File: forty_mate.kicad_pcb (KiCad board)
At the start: 2 copper layers, 247.5 x 76 mm, 95 parts, among them SW1 SW_Push, SW10 SW_Push, SW11 SW_Push, SW12 SW_Push, SW13 SW_Push, SW14 SW_Push, SW15 SW_Push, SW16 SW_Push, SW17 SW_Push, SW18 SW_Push, SW19 SW_Push, SW2 SW_Push, SW20 SW_Push, SW21 SW_Push, SW22 SW_Push, SW23 SW_Push, SW24 SW_Push, SW25 SW_Push, SW26 SW_Push, SW27 SW_Push, SW28 SW_Push, SW29 SW_Push, SW3 SW_Push, SW30 SW_Push, SW31 SW_Push, SW32 SW_Push, SW33 SW_Push, SW34 SW_Push, SW35 SW_Push, SW36 SW_Push, SW37 SW_Push, SW38 SW_Push, SW39 SW_Push, SW4 SW_Push, SW40 SW_Push, SW41 SW_Push, SW42 SW_Push, SW43 SW_Push, SW44 SW_SPDT, SW5 SW_Push, SW6 SW_Push, SW7 SW_Push, SW8 SW_Push, SW9 SW_Push, U1 Micon_BLEMicroPro

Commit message: gasket case version
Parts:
- added REF**: masro_poron, forty_mate:masro_poron, F.Cu at (260.6, 57.0)
- added REF**: masro_poron, forty_mate:masro_poron, F.Cu at (95.5, 57.0)
- added REF**: masro_poron, forty_mate:masro_poron, F.Cu at (80.5, 57.0)
- added REF**: masro_poron, forty_mate:masro_poron, F.Cu at (178.0, 138.2)
- added REF**: masro_poron, forty_mate:masro_poron, F.Cu at (178.0, 57.0)
- added REF**: masro_poron, forty_mate:masro_poron, F.Cu at (122.0, 138.2)
- added REF**: masro_poron, forty_mate:masro_poron, F.Cu at (204.6, 57.0)
- added REF**: masro_poron, forty_mate:masro_poron, F.Cu at (39.5, 57.0)
- added REF**: masro_poron, forty_mate:masro_poron, F.Cu at (54.5, 57.0)
- added REF**: masro_poron, forty_mate:masro_poron, F.Cu at (95.5, 138.2)
- added REF**: masro_poron, forty_mate:masro_poron, F.Cu at (163.0, 138.2)
- added REF**: masro_poron, forty_mate:masro_poron, F.Cu at (219.6, 57.0)
- added REF**: masro_poron, forty_mate:masro_poron, B.Cu at (69.5, 138.2)
- added REF**: masro_poron, forty_mate:masro_poron, F.Cu at (163.0, 57.0)
- added REF**: masro_poron, forty_mate:masro_poron, F.Cu at (137.0, 57.0)
- added REF**: masro_poron, forty_mate:masro_poron, F.Cu at (204.6, 138.2)
- added REF**: masro_poron, forty_mate:masro_poron, F.Cu at (137.0, 138.2)
- added REF**: masro_poron, forty_mate:masro_poron, F.Cu at (230.6, 138.2)
- added REF**: masro_poron, forty_mate:masro_poron, F.Cu at (245.6, 57.0)
- added REF**: masro_poron, forty_mate:masro_poron, F.Cu at (122.0, 57.0)
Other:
- board text added: "User1: general case plate line User2: split line User3: switch plate line User4: poron"
- board text removed: "User1: outline User2: outline 2 (split)"

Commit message: kari kansei
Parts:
- removed BT2: Battery_Cell, kbd_Parts:Battery_ali_CR1632
- removed C2: C_Polarized_Small, kbd_Parts:Capacitor_1206
- removed D45: D_Schottky, forty_mate:Diode_SMD
- removed G***: LOGO, forty_mate:Silk_Title
- removed the REF** at (260.6, 57.0)
- removed the REF** at (95.5, 57.0)
- removed the REF** at (80.5, 57.0)
- removed the REF** at (178.0, 138.2)
- removed the REF** at (178.0, 57.0)
- removed the REF** at (122.0, 138.2)
- removed the REF** at (204.6, 57.0)
- removed the REF** at (39.5, 57.0)
- removed the REF** at (54.5, 57.0)
- removed the REF** at (95.5, 138.2)
- removed the REF** at (163.0, 138.2)
- removed the REF** at (219.6, 57.0)
- removed the REF** at (69.5, 138.2)
- removed the REF** at (163.0, 57.0)
- removed the REF** at (137.0, 57.0)
- removed the REF** at (204.6, 138.2)
- removed the REF** at (137.0, 138.2)
- removed the REF** at (230.6, 138.2)
- removed the REF** at (245.6, 57.0)
- removed the REF** at (122.0, 57.0)
- added REF**: MountingHole_2.1mm, MountingHole:MountingHole_2.1mm, F.Cu at (59.5, 133.3)
- added REF**: MountingHole_2.1mm, MountingHole:MountingHole_2.1mm, F.Cu at (107.2, 116.7)
- added REF**: MountingHole_2.1mm, MountingHole:MountingHole_2.1mm, F.Cu at (50.0, 97.6)
- added REF**: MountingHole_2.1mm, MountingHole:MountingHole_2.1mm, F.Cu at (235.7, 119.1)
- added REF**: MountingHole_2.1mm, MountingHole:MountingHole_2.1mm, F.Cu at (59.5, 119.1)
- added REF**: MountingHole_2.1mm, MountingHole:MountingHole_2.1mm, F.Cu at (242.9, 97.6)
- added REF**: MountingHole_2.1mm, MountingHole:MountingHole_2.1mm, F.Cu at (235.7, 133.3)
- added REF**: MountingHole_2.1mm, MountingHole:MountingHole_2.1mm, F.Cu at (188.1, 116.7)
- added SW45: SW_Push, kbd_Parts:ResetSW, F.Cu at (235.7, 126.2)
- C1, SW44: moved to B.Cu
- D44: footprint forty_mate:Diode_SMD -> forty_mate:Diode_SMD_S-FLAT
- SW12, SW35, SW38: footprint kbd_SW:CherryMX_Hotswap_1u -> kbd_SW:CherryMX_Hotswap_1.25u
- SW14, SW39: footprint kbd_SW:CherryMX_Hotswap_1.25u -> kbd_SW:CherryMX_Hotswap_1u
- SW23, SW43: footprint kbd_SW:CherryMX_Hotswap_1u -> kbd_SW:CherryMX_Hotswap_1.75u
- SW25, SW26: footprint kbd_SW:CherryMX_Hotswap_1.75u -> kbd_SW:CherryMX_Hotswap_1u
- SW36: footprint kbd_SW:CherryMX_Hotswap_1u -> kbd_SW:CherryMX_Hotswap_2u_Rev
- SW37: footprint kbd_SW:CherryMX_Hotswap_1.25u -> kbd_SW:CherryMX_Hotswap_2.25u_Rev
- SW40: footprint kbd_SW:CherryMX_Hotswap_2u_Rev -> kbd_SW:CherryMX_Hotswap_1u
- SW41: footprint kbd_SW:CherryMX_Hotswap_2.25u_Rev -> kbd_SW:CherryMX_Hotswap_1u
- moved SW44 243.6 mm to (271.5, 126.2)
- moved BT1 216.7 mm to (45.2, 126.2), turned to 0 degrees
- moved U1 209.5 mm to (254.8, 126.2), turned to -90 degrees
- moved SW12 208.0 mm to (38.1, 88.1)
- moved D12 208.0 mm to (45.2, 92.9)
- moved SW13 205.7 mm to (59.5, 88.1)
- moved D13 205.7 mm to (66.7, 92.9)
- moved C1 196.4 mm to (258.6, 128.6), turned to 180 degrees
- moved SW23 170.1 mm to (42.9, 107.2)
- moved SW25 170.1 mm to (88.1, 107.2)
- moved D25 170.1 mm to (95.2, 111.9)
- moved D23 170.1 mm to (50.0, 111.9)
- moved SW24 163.0 mm to (69.1, 107.2)
- moved D24 163.0 mm to (76.2, 111.9)
- moved SW34 130.0 mm to (73.8, 126.2)
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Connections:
- D12 pad 1: row0 -> row1
- D13 pad 1: row0 -> row1
- D23 pad 1: row1 -> row2
- D24 pad 1: row1 -> row2
- D25 pad 1: row1 -> row2
- D34 pad 1: row2 -> row3
- D35 pad 1: row2 -> row3
- D36 pad 1: row2 -> row3
- D37 pad 1: row2 -> row3
- SW12 pad 1: col11 -> col0
- SW13 pad 1: col12 -> col1
- SW14 pad 1: col0 -> col2
- SW15 pad 1: col1 -> col3
- SW16 pad 1: col2 -> col4
- SW17 pad 1: col3 -> col5
- SW18 pad 1: col4 -> col6
- SW19 pad 1: col5 -> col7
- SW20 pad 1: col6 -> col8
- SW21 pad 1: col7 -> col9
- SW22 pad 1: col8 -> col10
- SW23 pad 1: col9 -> col0
- SW24 pad 1: col10 -> col1
- SW25 pad 1: col12 -> col2
- SW26 pad 1: col0 -> col3
- SW27 pad 1: col2 -> col4
- SW28 pad 1: col3 -> col5
- SW29 pad 1: col4 -> col6
- SW30 pad 1: col5 -> col7
- SW31 pad 1: col6 -> col8
- SW32 pad 1: col7 -> col9
- SW33 pad 1: col8 -> col10
- SW34 pad 1: col9 -> col1
- SW35 pad 1: col10 -> col2
- SW36 pad 1: col11 -> col3
- SW37 pad 1: col12 -> col4
- SW38 pad 1: col2 -> col5
- SW39 pad 1: col3 -> col6
- SW40 pad 1: col5 -> col7
- SW41 pad 1: col7 -> col8
- U1 pad 10: col10 -> col9
- U1 pad 11: col11 -> col8
- U1 pad 12: col12 -> col7
- U1 pad 13: col3 -> unconnected-(U1-Pad13)
- U1 pad 14: col2 -> col0
- U1 pad 16: col0 -> col2
- U1 pad 2: col4 -> unconnected-(U1-Pad2)
- U1 pad 22: unconnected-(U1-Pad22) -> reset
- U1 pad 5: col5 -> col6
- U1 pad 6: col6 -> col5
- U1 pad 7: col7 -> col4
- U1 pad 8: col8 -> col3
- U1 pad 9: col9 -> col10
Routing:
- net col12: track 272.5 -> 0.00 mm, vias 7 -> 0
- net GND: track 0.00 -> 260.3 mm, vias 7 -> 0
- net col11: track 249.4 -> 0.00 mm, vias 6 -> 0
- net col3: track 104.2 -> 329.4 mm, vias 4 -> 6
- net col1: track 58.6 -> 282.0 mm, vias 2 -> 5
- net Net-(D44-Pad1): track 230.3 -> 10.5 mm, vias 3 -> 0
- net Net-(BT1-Pad1): track 26.3 -> 231.9 mm
- net col0: track 74.5 -> 278.2 mm, vias 3 -> 4
- net col2: track 101.4 -> 265.3 mm, vias 4 -> 5
- net col4: track 177.8 -> 324.8 mm, vias 5 -> 6
- net col9: track 269.8 -> 123.7 mm, vias 6 -> 5
- net col10: track 261.4 -> 143.9 mm, vias 8 -> 4
- net col8: track 227.9 -> 116.2 mm, vias 5 -> 4
- net col5: track 213.2 -> 318.6 mm
- net col6: track 207.5 -> 306.1 mm, vias 5 -> 6
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- removed copper zone on B.Cu, net GND
- removed copper zone on F.Cu, net GND

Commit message: karikansei2
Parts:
- added REF**: MountingHole_2.1mm, MountingHole:MountingHole_2.1mm, F.Cu at (188.1, 78.6)
- added REF**: MountingHole_2.1mm, MountingHole:MountingHole_2.1mm, F.Cu at (107.2, 78.6)
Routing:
- net col3: track 329.4 -> 331.4 mm
- net col4: track 324.8 -> 326.6 mm
- net col5: track 318.6 -> 319.7 mm
- net col6: track 306.1 -> 307.2 mm
- net row0: track 298.5 -> 299.2 mm

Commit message: temporal progress
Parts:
- moved D43 14.3 mm to (264.3, 92.9)
- moved REF** 4.76 mm to (247.7, 97.6)
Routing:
- net col3: track 331.4 -> 156.3 mm
- net col4: track 326.6 -> 169.4 mm
- net col5: track 319.7 -> 180.7 mm
- net col6: track 307.2 -> 214.2 mm
- net Net-(D43-Pad2): track 21.4 -> 8.95 mm
- net row3: track 258.9 -> 269.4 mm
- net row2: track 322.6 -> 321.5 mm
- net row0: track 299.2 -> 298.5 mm

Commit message: second prototype
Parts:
- added REF**: MountingHole_2.1mm, MountingHole:MountingHole_2.1mm, F.Cu at (145.3, 97.6)
- moved REF** 20.3 mm to (240.5, 78.6)
- moved REF** 19.0 mm to (50.0, 78.6)
- moved D43 14.3 mm to (250.0, 92.9)
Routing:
- net col3: track 156.3 -> 332.6 mm
- net col4: track 169.4 -> 327.6 mm
- net col5: track 180.7 -> 320.9 mm
- net col6: track 214.2 -> 308.3 mm
- net Net-(D43-Pad2): track 8.95 -> 21.4 mm
- net row3: track 269.4 -> 258.9 mm
- net col10: track 143.9 -> 141.2 mm
- net row1: track 312.6 -> 313.4 mm
- net row0: track 298.5 -> 299.2 mm
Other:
- board size 247.5 x 76 mm -> 247.7 x 76.2 mm

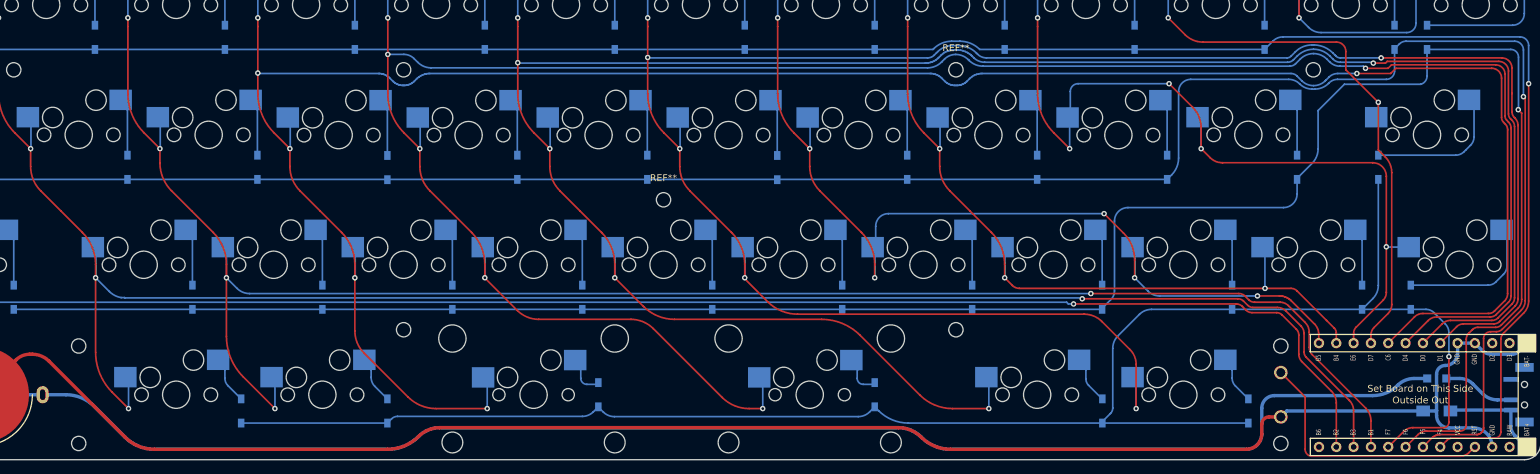
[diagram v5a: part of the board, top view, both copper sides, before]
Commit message: tiny mod (ref text of screw hole)
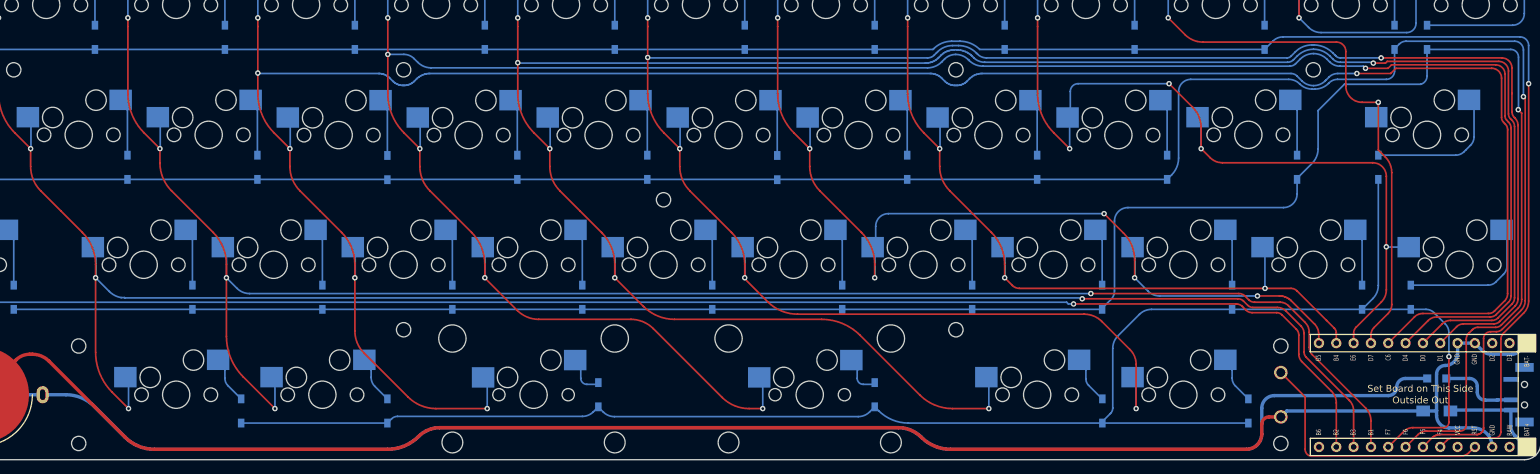
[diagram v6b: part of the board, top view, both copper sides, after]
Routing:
- net col10: track 141.2 -> 142.9 mm
- net Net-(D44-Pad1): track 10.5 -> 11.6 mm
- net Net-(BT1-Pad1): track 231.9 -> 232.6 mm

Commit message: add switch-plate and more change (true second proto) micon is inside out. changed cell box. switch no tokoro egutte mita
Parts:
- BT1: footprint kbd_Parts:Battery_ali_CR1632 -> forty_mate:HU1632
- U1: footprint kbd_Parts:Micon_BMP_7sKB -> kbd_Parts:Micon_BMP_N60
- moved D44 5.59 mm to (258.6, 129.4)
- moved C1 5.40 mm to (258.6, 123.2)
- moved BT1 2.38 mm to (42.9, 126.2)
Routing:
- net row3: track 258.9 -> 234.4 mm, vias 1 -> 0
- net col3: track 332.6 -> 352.8 mm
- net col4: track 327.6 -> 347.6 mm
- net col5: track 320.9 -> 340.6 mm
- net col6: track 308.3 -> 327.7 mm
- net col7: track 141.2 -> 157.3 mm
- net col8: track 116.2 -> 132.0 mm
- net col10: track 142.9 -> 158.4 mm
- net col9: track 123.6 -> 138.8 mm
- net row0: track 299.2 -> 284.5 mm, vias 1 -> 0
- net row1: track 313.4 -> 299.7 mm, vias 1 -> 0
- net row2: track 321.1 -> 307.9 mm, vias 1 -> 0
- net col1: track 282.0 -> 270.0 mm, vias 5 -> 6
- net col0: track 278.2 -> 266.2 mm, vias 4 -> 5
- net col2: track 265.3 -> 254.2 mm, vias 5 -> 6
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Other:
- outline, holes or cut-outs redrawn

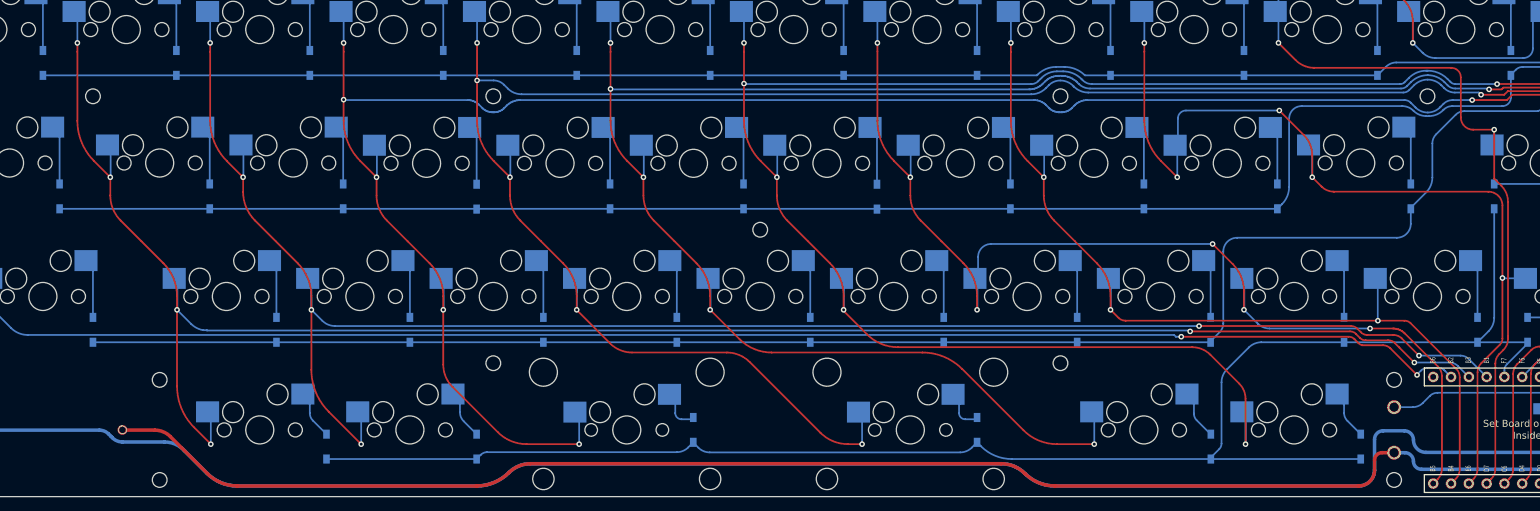
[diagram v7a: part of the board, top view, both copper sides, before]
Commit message: change screw hole placement
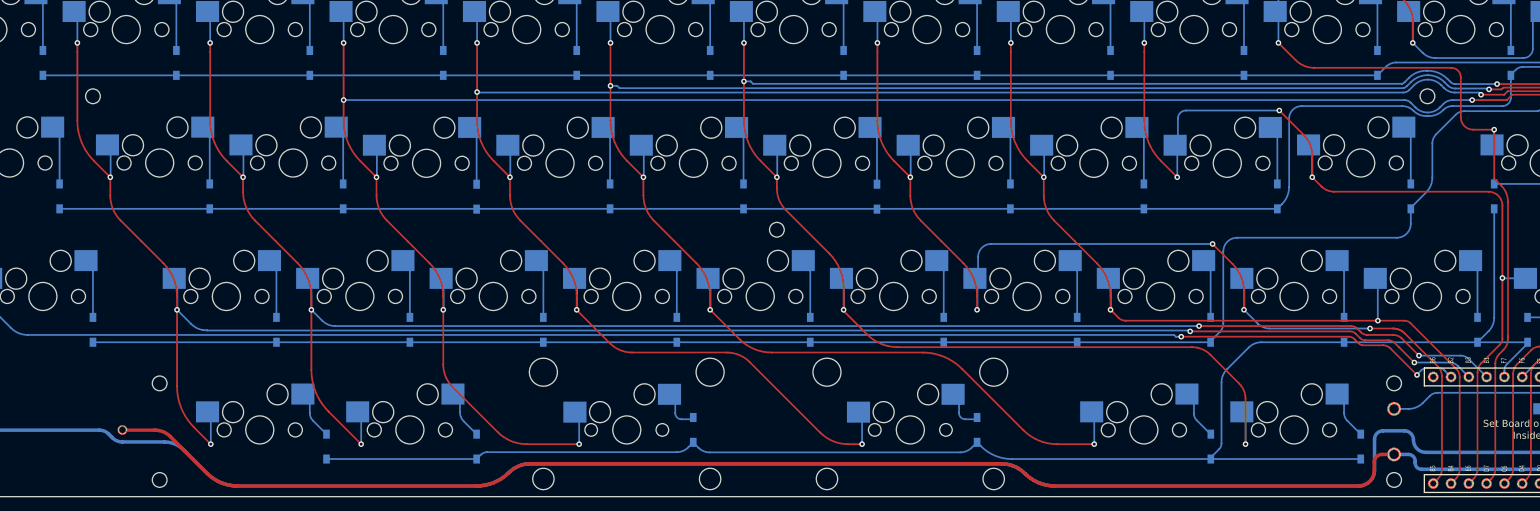
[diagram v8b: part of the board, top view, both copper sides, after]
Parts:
- removed the REF** at (188.1, 116.7)
- removed the REF** at (188.1, 78.6)
- removed the REF** at (107.2, 116.7)
- removed the REF** at (107.2, 78.6)
- moved REF** 2.38 mm to (147.6, 97.6)
- moved REF** 0.50 mm to (235.7, 119.6)
- moved REF** 0.50 mm to (59.5, 119.6)
- moved SW45 0.25 mm to (235.7, 126.5)
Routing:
- net col3: track 352.8 -> 350.6 mm
- net col4: track 347.6 -> 346.1 mm
- net col5: track 340.6 -> 339.6 mm
- net col6: track 327.7 -> 326.8 mm
- net row0: track 284.5 -> 283.9 mm
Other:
- board text added: "User1: general case plate line User3: switch plate line User4: poron"
- board text removed: "User1: general case plate line User2: split line User3: switch plate line User4: poron"
